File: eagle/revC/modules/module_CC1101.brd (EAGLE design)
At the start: 24.1 x 32.8 mm, 14 parts, among them X1 734120110

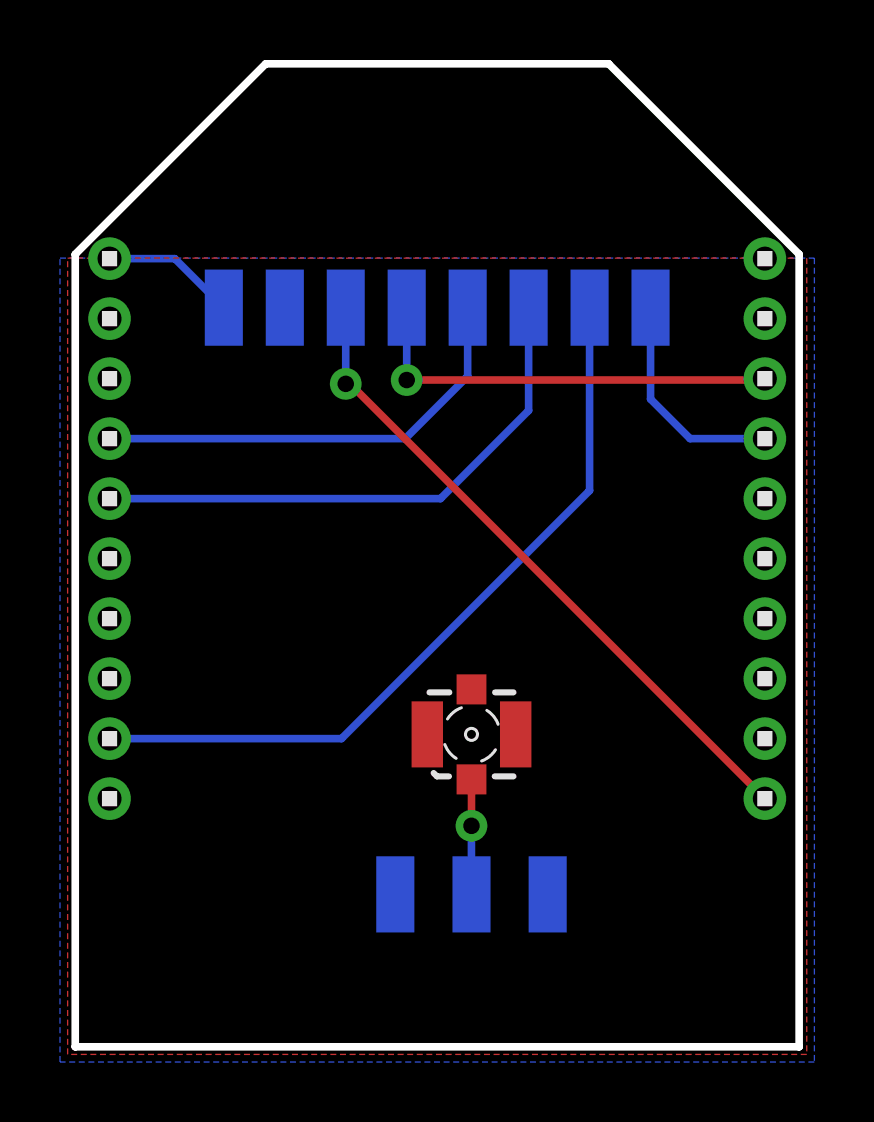
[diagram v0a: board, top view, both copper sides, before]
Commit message: Replaced modules with library parts
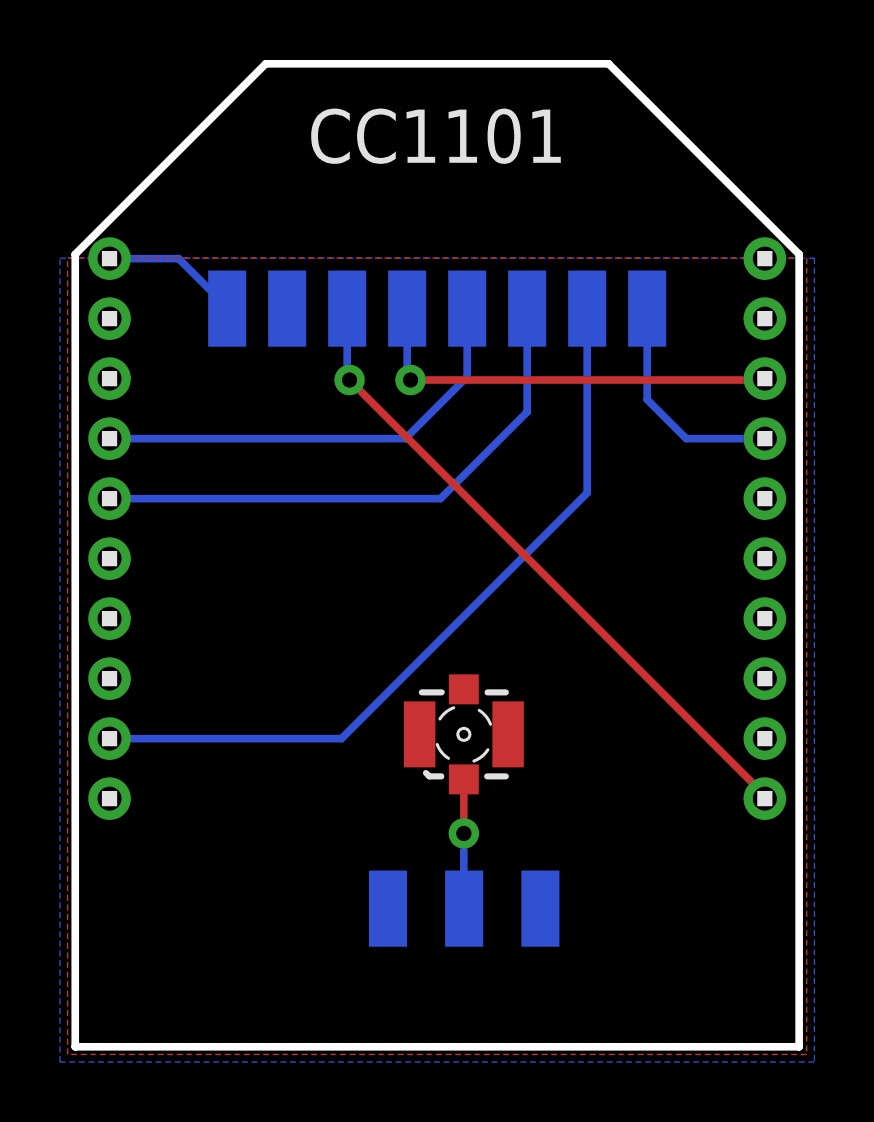
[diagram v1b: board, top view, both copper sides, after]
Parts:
- removed 3.3V, ANT, GDO0, GDO2, GND, GND_ANT, GND_ANT1, MISO, MOSI, NSS, SCK: (no value), wirepad:SMD1,27-2,54
- added CC1101: CC1101, RadioShield:CC1101
- moved X1 0.25 mm to (13.1, 10.5)
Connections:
- removed net ANT: ANT.1, X1.1
- new net N$1: CC1101.ANT, X1.1
- net GND: now also CC1101.GND@1, CC1101.GND@2, CC1101.GND@3; no longer GND.1, GND_ANT.1, GND_ANT1.1
- net INT0: now also CC1101.GDO0; no longer GDO0.1
- net INT1: now also CC1101.GDO2; no longer GDO2.1
- net SPI_CS: now also CC1101.CS; no longer NSS.1
- net SPI_MISO: now also CC1101.MISO; no longer MISO.1
- net SPI_MOSI: now also CC1101.MOSI; no longer MOSI.1
- net SPI_SCK: now also CC1101.SCK; no longer SCK.1
- net VCC: now also CC1101.VCC; no longer 3.3V.1
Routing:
- net N$1: track 0.00 -> 4.31 mm, vias 0 -> 1
- net ANT: track 3.83 -> 0.00 mm, vias 1 -> 0
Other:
- board text removed: "3.3V"
- board text removed: "ANT"
- board text removed: "GDO0"
- board text removed: "GDO2"
- board text removed: "GND"
- board text removed: "MISO"
- board text removed: "MOSI"
- board text removed: "NSS"
- board text removed: "SCK"
